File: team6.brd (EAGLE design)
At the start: 47 x 28 mm, 51 parts, among them IC1 MCP1252-33X50, J1 FTDI_DEVICE, M1 WIRELESS-NRF24L01, Q1 BSS123, Q2 BSS123, Q3 BSS123, Q4 BSS123, U1 ATMEGA328P_TQFP, U3 GY-521MPU6050, Y1 8MHz

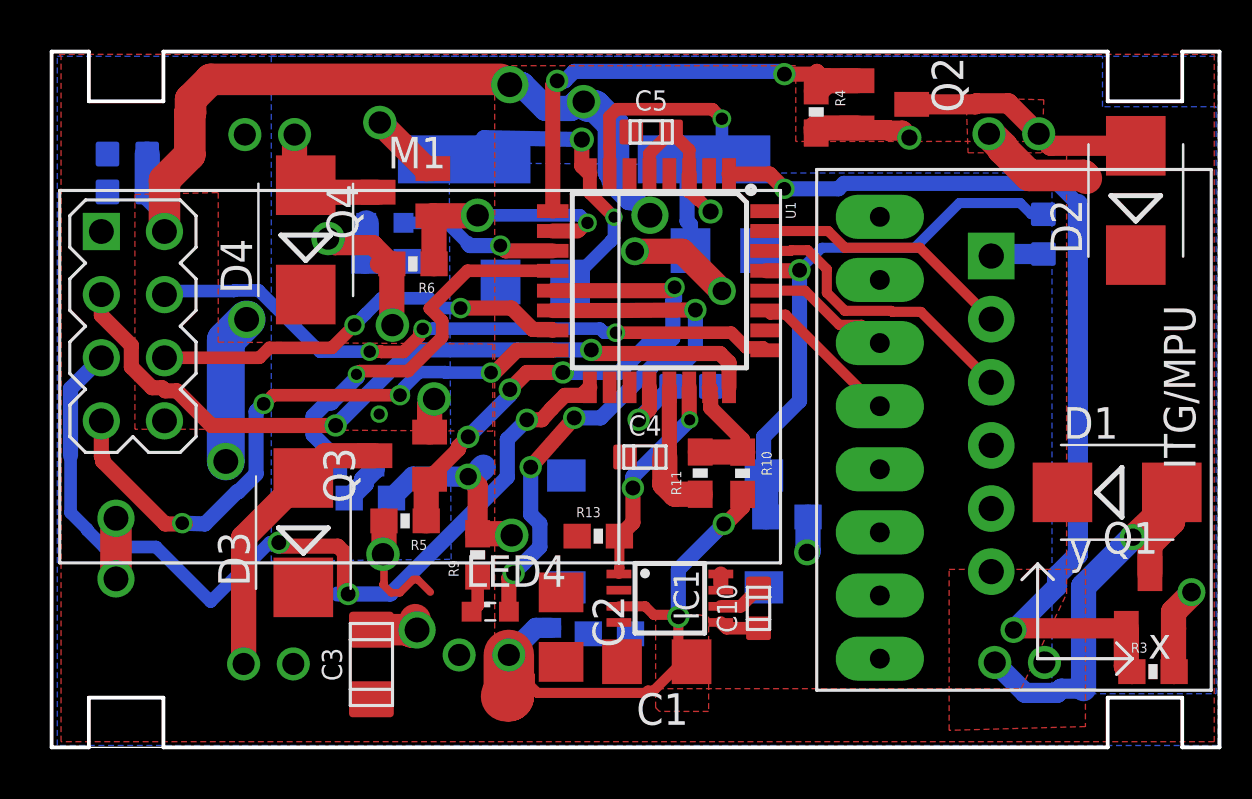
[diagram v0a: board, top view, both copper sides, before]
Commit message: renamed files
renamed files and one airwire left
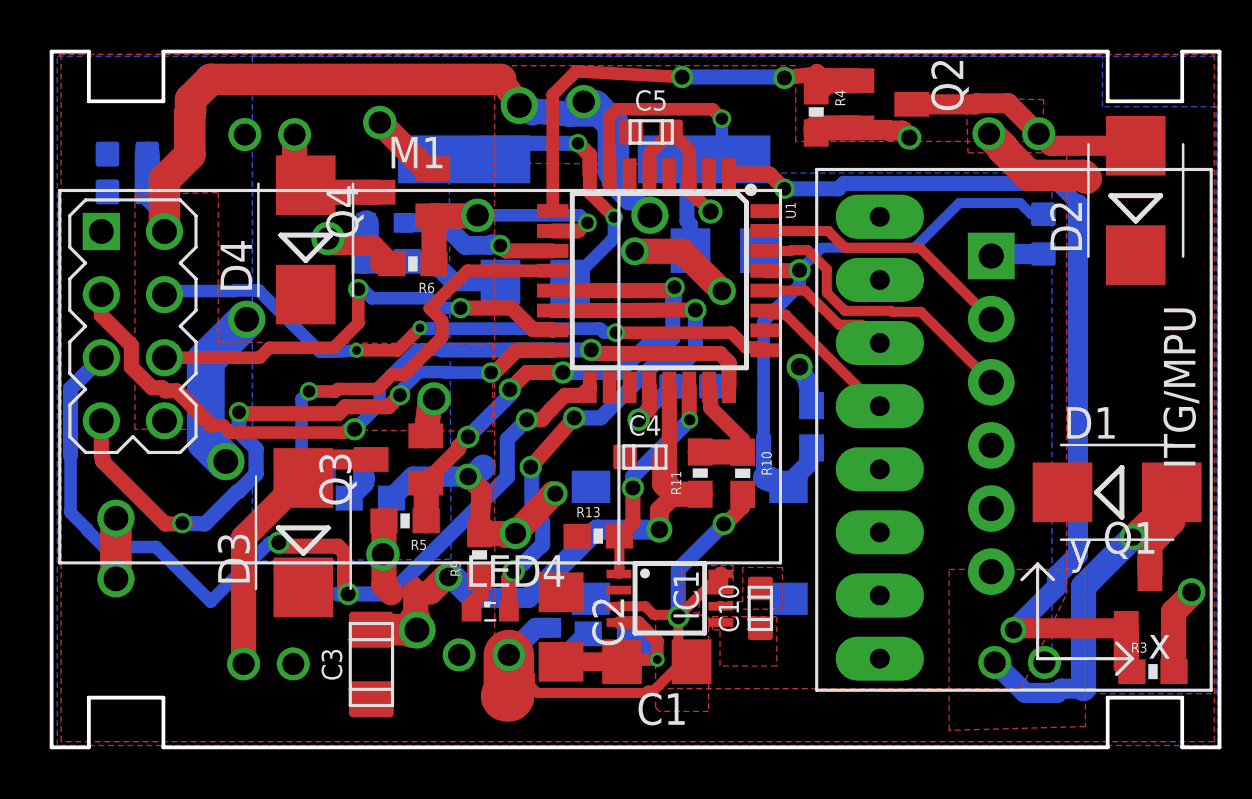
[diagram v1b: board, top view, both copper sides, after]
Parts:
- moved R1 3.76 mm to (30.6, 12.9), turned to 90 degrees
- moved S1 1.09 mm to (25.7, 8.23)
- moved LED3 0.48 mm to (11.8, 11.2)
- moved Q3 0.22 mm to (14.0, 11.6)
- moved C10 0.08 mm to (28.5, 5.59)
- moved R9 0.08 mm to (17.2, 7.75)
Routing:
- net DGND: track 22.3 -> 40.0 mm, vias 8 -> 10
- net AGND: track 5.56 -> 18.2 mm, vias 0 -> 2
- net 3.7V: track 34.1 -> 37.2 mm
- net MGND: track 21.4 -> 19.1 mm, vias 7 -> 6
- net RESET: track 23.1 -> 25.3 mm
- net 3.3V: track 33.8 -> 36.0 mm
- net N$5: track 0.00 -> 2.01 mm
- net N$12: track 1.82 -> 0.00 mm
- net N$11: track 1.61 -> 0.00 mm
- net LED_2: track 16.0 -> 17.1 mm
- net MOSI: track 17.2 -> 18.3 mm
- net MISO: track 25.6 -> 26.6 mm
- net GND: track 1.65 -> 0.79 mm
- net CE: track 30.9 -> 31.6 mm
- added copper zone on layer 1, net N$11
- added copper zone on layer 1, net N$12

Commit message: version 3 board design
component placement done
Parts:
- moved U$8 84.0 mm to (-39.4, 71.1)
- moved U$7 82.4 mm to (-36.8, 71.1), turned to 0 degrees
- moved U$6 81.6 mm to (-34.3, 71.1)
- moved D2 41.0 mm to (4.57, 9.53), flipped to the bottom, turned to 0 degrees
- moved U$3 40.8 mm to (2.46, 6.10), flipped to the top, turned to 180 degrees
- moved Q2 27.0 mm to (14.1, 7.11), flipped to the bottom
- moved R7 26.4 mm to (39.0, 26.3), flipped to the top, turned to 0 degrees
- moved R4 23.1 mm to (14.2, 9.53), flipped to the bottom, turned to 0 degrees
- moved LED2 22.7 mm to (35.6, 26.3), flipped to the top
- moved LED4 22.1 mm to (9.27, 25.9)
- moved U$4 21.3 mm to (8.52, 3.34), flipped to the top, turned to 90 degrees
- moved J1 19.7 mm to (22.6, 25.9), flipped to the top, turned to 180 degrees
- moved C10 19.3 mm to (12.6, 16.5)
- moved R9 18.8 mm to (8.38, 24.4), turned to 0 degrees
- moved C1 17.7 mm to (16.1, 19.2), turned to 0 degrees
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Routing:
- net DGND: track 40.0 -> 0.00 mm, vias 10 -> 0
- net MOTOR_1: track 39.4 -> 0.00 mm, vias 2 -> 0
- net 3.7V: track 37.2 -> 0.00 mm, vias 4 -> 0
- net SCK: track 36.8 -> 0.00 mm, vias 3 -> 0
- net 3.3V: track 36.0 -> 0.00 mm, vias 4 -> 0
- net CE: track 31.6 -> 0.00 mm, vias 2 -> 0
- net MISO: track 26.6 -> 0.00 mm, vias 4 -> 0
- net CSN: track 26.3 -> 0.00 mm, vias 3 -> 0
- net RESET: track 25.3 -> 0.00 mm, vias 1 -> 0
- net LED_3: track 23.0 -> 0.00 mm, vias 4 -> 0
- net MOTOR_4: track 21.2 -> 0.00 mm, vias 4 -> 0
- net MGND: track 19.1 -> 0.00 mm, vias 6 -> 0
- net MOSI: track 18.3 -> 0.00 mm, vias 2 -> 0
- net AGND: track 18.2 -> 0.00 mm, vias 2 -> 0
- net MOTOR_2: track 18.1 -> 0.00 mm, vias 2 -> 0
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- removed copper zone on layer 1, net 3.3V
- removed copper zone on layer 1, net 3.7V
- removed copper zone on layer 16, net DGND
- removed copper zone on layer 16, net MGND
- removed copper zone on layer 1, net N$11
- removed copper zone on layer 1, net N$12
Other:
- board size 47 x 28 mm -> 100 x 80 mm
